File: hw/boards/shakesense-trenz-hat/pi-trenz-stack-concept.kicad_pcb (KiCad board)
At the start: 8 copper layers, 85 x 56 mm, 102 parts, among them J1 Raspberry Pi 40-pin, J2 Passive GNSS antenna, J4 FPGA test UART/reset, J80 LSHM-150-04.0-L-DV-A-S-K-TR, J81 LSHM-150-04.0-L-DV-A-S-K-TR, J82 LSHM-130-04.0-L-DV-A-S-K-TR, J83 1715721, J84 TSW-106-07-G-S, J85 TSW-103-07-G-D, J86 BANK13 / 40p FFC, J87 BANK14 / 40p FFC, J88 BANK15 / 60p FFC, J89 BANK16 / 60p FFC, Q1 2N7002, U1 24LC32A, U11 LSM6DSOTR, U12 LSM6DSOTR, U13 LSM6DSOTR, U14 LSM6DSOTR, U20 SCL3300-D01, U21 MAX-M10S, U40 TLV1117LV33DCYR, U41 SN74LVC8T245PWR, U42 SN74LVC8T245PWR, U43 ISO1640BDR, U51 TXU0202DCUR, U52 TLV803EA30DBZR

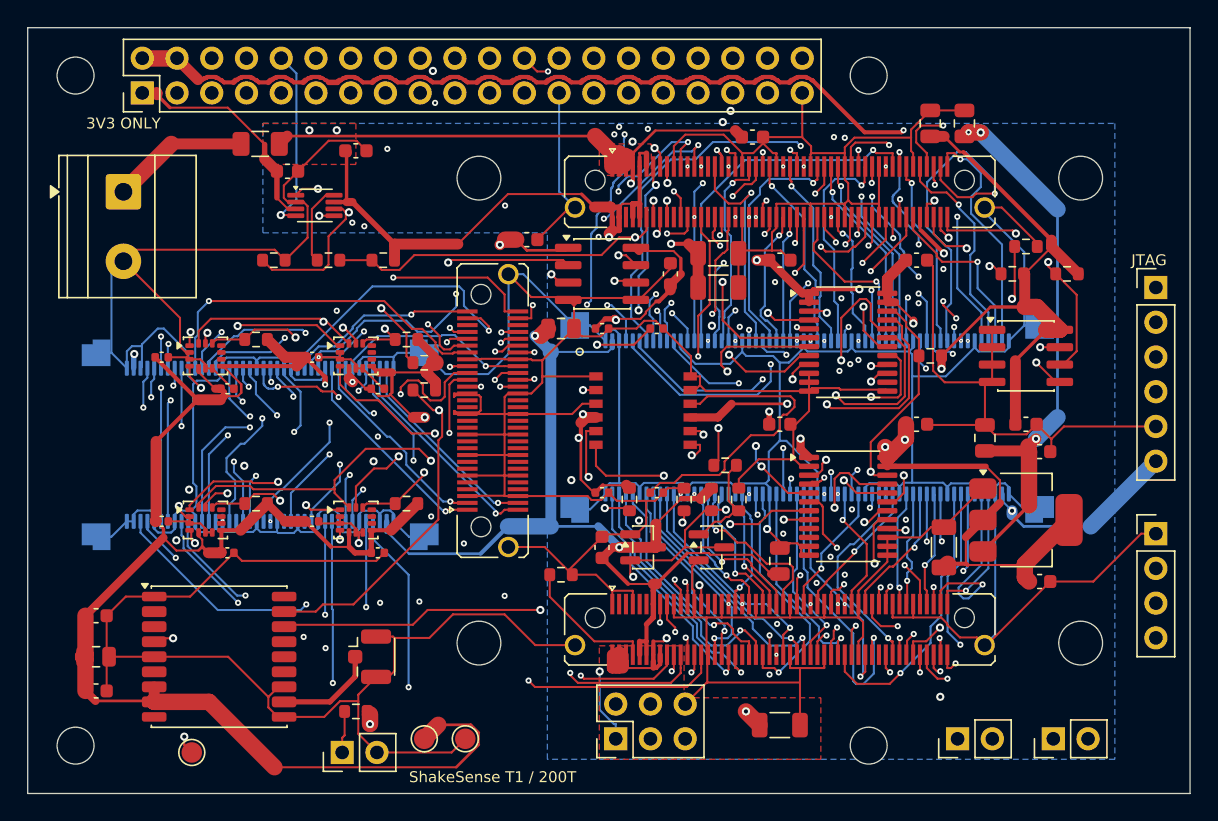
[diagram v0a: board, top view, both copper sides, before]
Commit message: Replace T1 GNSS with single Racotech geophone input
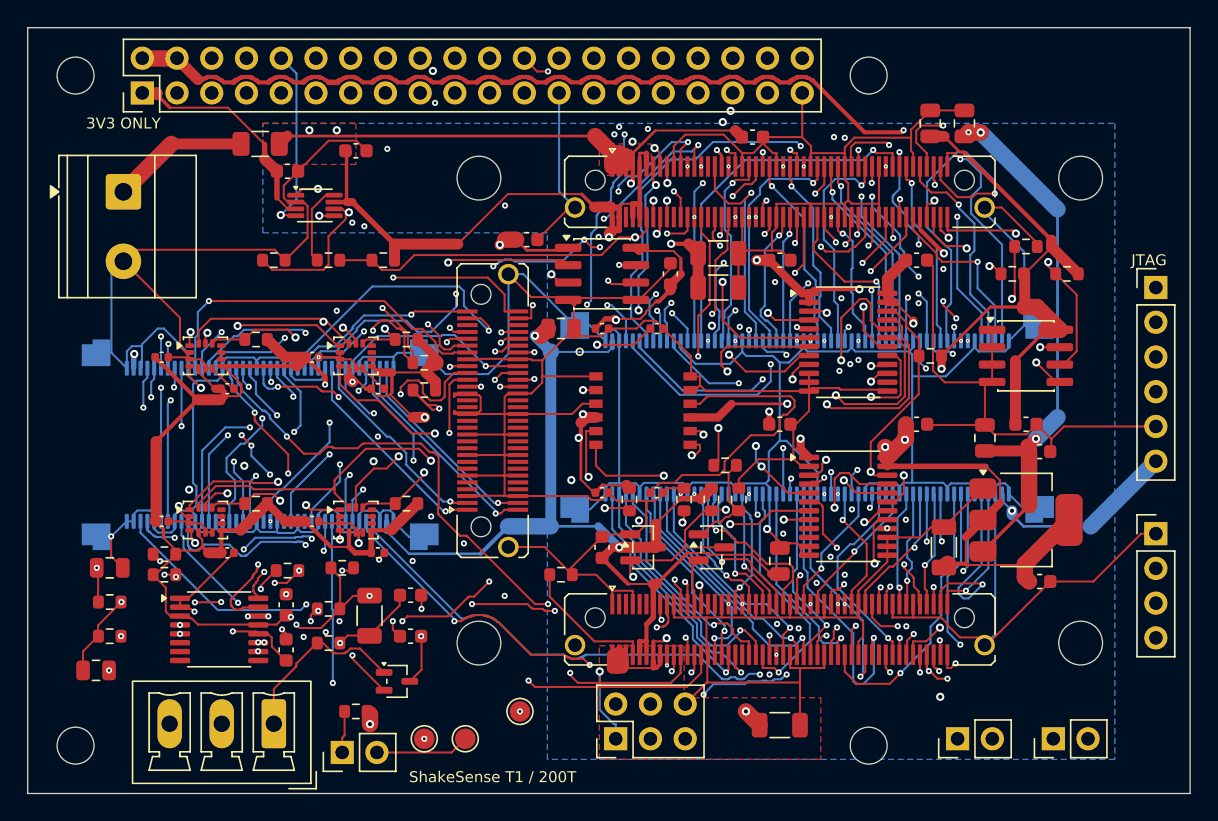
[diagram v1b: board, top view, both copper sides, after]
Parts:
- removed C24, C26: 100n, ShakeSense:Capacitor_SMD__C_0603_1608Metric
- removed C25: 4.7u, ShakeSense:Capacitor_SMD__C_0805_2012Metric
- removed J2: Passive GNSS antenna, ShakeSense:Connector_Coaxial__U.FL_Hirose_U.FL-R-SMT-1_Vertical
- removed U21: MAX-M10S, ShakeSense:RF_GPS__ublox_MAX
- added C90: 100n C0G, ShakeSense:Capacitor_SMD__C_1206_3216Metric, F.Cu at (75.0, 93.0)
- added C91: 1n C0G, ShakeSense:Capacitor_SMD__C_0603_1608Metric, F.Cu at (78.0, 91.5)
- added C92: 1n C0G, ShakeSense:Capacitor_SMD__C_0603_1608Metric, F.Cu at (78.0, 94.5)
- added C93: 10u, ShakeSense:Capacitor_SMD__C_0805_2012Metric, F.Cu at (55.0, 97.0)
- added C94: 10u, ShakeSense:Capacitor_SMD__C_0805_2012Metric, F.Cu at (56.0, 89.5)
- added C95: 100n, ShakeSense:Capacitor_SMD__C_0603_1608Metric, F.Cu at (68.9, 95.5)
- added C96: 100n, ShakeSense:Capacitor_SMD__C_0603_1608Metric, F.Cu at (68.9, 92.2)
- added D90: TPD2E2U06, ShakeSense:Package_TO_SOT_SMD__SOT-323_SC-70, F.Cu at (77.0, 97.8)
- added J90: GEO + / - / SHIELD, ShakeSense:Connector_Phoenix_MC__PhoenixContact_MCV_1,5_3-G-3.81_1x03_P3.81mm_Vertical, F.Cu at (68.0, 100.9)
- added R90: 1k, ShakeSense:Resistor_SMD__R_0603_1608Metric, F.Cu at (72.0, 95.0)
- added R91: 1k, ShakeSense:Resistor_SMD__R_0603_1608Metric, F.Cu at (72.0, 92.5)
- added R92: 1M, ShakeSense:Resistor_SMD__R_0603_1608Metric, F.Cu at (69.0, 89.7)
- added R93: 1M, ShakeSense:Resistor_SMD__R_0603_1608Metric, F.Cu at (73.0, 89.5)
- added R94: 10k, ShakeSense:Resistor_SMD__R_0603_1608Metric, F.Cu at (56.0, 92.0)
- added R95: 10k, ShakeSense:Resistor_SMD__R_0603_1608Metric, F.Cu at (56.0, 94.5)
- added R96: 22, ShakeSense:Resistor_SMD__R_0603_1608Metric, F.Cu at (60.0, 90.0)
- added R97: 10k, ShakeSense:Resistor_SMD__R_0603_1608Metric, F.Cu at (60.0, 88.5)
- added U22: ADS122C04, ShakeSense:Package_SO__TSSOP-16_4.4x5mm_P0.65mm, F.Cu at (64.0, 94.0)
- moved TP4 24.2 mm to (86.0, 100.0)
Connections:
- net PI_GNSS_PPS renamed PI_GEO_DRDY_N
- U42 pad 16: GNSS_PPS -> GEO_DRDY_N
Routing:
- net GEO_DRDY_N: track 0.00 -> 66.6 mm, vias 0 -> 7
- net GNSS_PPS: track 61.5 -> 0.00 mm, vias 2 -> 0
- net GND: track 873.3 -> 819.5 mm, vias 5 -> 16
- net FPGA_B14_L18_P: track 60.1 -> 107.0 mm, vias 2 -> 4
- net SENSOR_OE_N: track 119.2 -> 85.3 mm, vias 3 -> 2
- net GEO_VCM: track 0.00 -> 24.6 mm, vias 0 -> 6
- net SENS_3V3: track 262.7 -> 240.1 mm, vias 10 -> 13
- net GEO_AVDD: track 0.00 -> 19.9 mm, vias 0 -> 4
- net GEO_N: track 0.00 -> 19.5 mm, vias 0 -> 3
- net GEO_AIN_P: track 0.00 -> 18.3 mm, vias 0 -> 4
- net GEO_AIN_N: track 0.00 -> 17.4 mm, vias 0 -> 4
- net I2C_SDA: track 76.0 -> 59.4 mm, vias 3 -> 7
- net GEO_P: track 0.00 -> 13.3 mm
- net FPGA_B14_L24_P: track 73.6 -> 65.6 mm, vias 2 -> 4
- net GNSS_RF: track 7.42 -> 0.00 mm
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
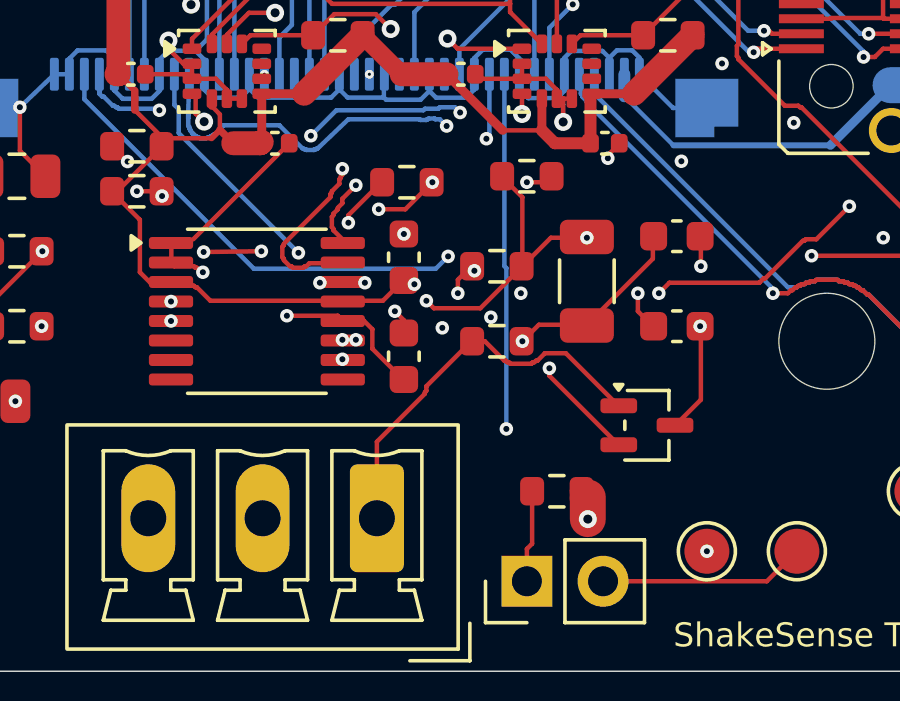
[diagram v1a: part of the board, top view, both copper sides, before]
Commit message: Harden geophone acquisition and tighten analog layout
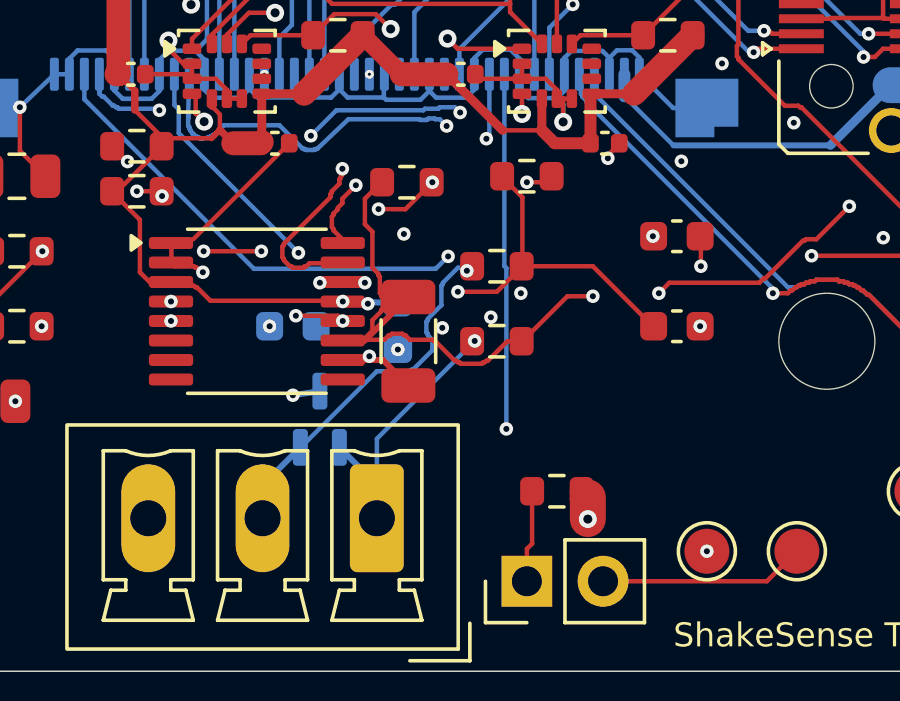
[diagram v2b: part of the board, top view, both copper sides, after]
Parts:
- C95, C96, D90: moved to B.Cu
- moved D90 10.9 mm to (66.1, 97.6), turned to 90 degrees
- moved C90 6.28 mm to (69.0, 95.0), turned to -90 degrees
- moved C95 3.83 mm to (65.2, 94.5), turned to 180 degrees
- moved C96 2.31 mm to (68.7, 94.5), turned to -90 degrees
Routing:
- net GND: track 819.5 -> 813.0 mm, vias 16 -> 18
- net GEO_N: track 19.5 -> 14.3 mm, vias 3 -> 1
- net GEO_P: track 13.3 -> 9.19 mm, vias 0 -> 1
- net GEO_AIN_P: track 18.3 -> 20.8 mm, vias 4 -> 2
- net GEO_AVDD: track 19.9 -> 17.4 mm, vias 4 -> 5
- net SENS_3V3: track 240.1 -> 241.4 mm, vias 13 -> 14
- net GEO_AIN_N: track 17.4 -> 18.0 mm, vias 4 -> 2

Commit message: Resolve T1 ribbon clearance with guided flex and windowed support
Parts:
- added MODEL_OFFSET_SPACER: Visualization only, , F.Cu at (50.0, 50.0)
- moved J87 3.00 mm to (67.0, 86.0)
- moved J83 2.30 mm to (54.7, 62.0)
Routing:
- net GND: track 813.0 -> 868.5 mm, vias 18 -> 30
- net FPGA_B14_L4_N: track 49.4 -> 82.5 mm, vias 3 -> 7
- net FPGA_B13_L6_P: track 44.1 -> 59.4 mm
- net FPGA_B14_L4_P: track 49.6 -> 64.1 mm, vias 2 -> 4
- net FPGA_3V3: track 227.7 -> 241.5 mm, vias 6 -> 8
- net FPGA_B14_L11_P: track 42.6 -> 53.5 mm, vias 3 -> 5
- net FPGA_B14_L5_P: track 22.1 -> 31.4 mm
- net FPGA_B13_L3_P: track 51.8 -> 60.8 mm, vias 6 -> 5
- net FPGA_B14_L14_P: track 57.6 -> 48.9 mm, vias 3 -> 5
- net FPGA_B14_L18_N: track 59.2 -> 66.7 mm, vias 2 -> 5
- net FPGA_B14_L18_P: track 107.0 -> 112.0 mm, vias 4 -> 6
- net FPGA_B14_L9_N: track 58.3 -> 62.2 mm
- net FPGA_B14_L9_P: track 57.4 -> 61.2 mm
- net FPGA_B14_L24_N: track 66.8 -> 70.3 mm
- net FPGA_B14_L15_P: track 53.5 -> 50.1 mm
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
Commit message: Implement internal Pi FPGA link and remove ribbon expansion
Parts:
- removed J84: TSW-106-07-G-S, ShakeSense:TZ_TZ_JTAG
- removed J85: TSW-103-07-G-D, ShakeSense:TZ_TZ_AUX
- removed J86: BANK13 / 40p FFC, ShakeSense:TZ_FFC40
- removed J87: BANK14 / 40p FFC, ShakeSense:TZ_FFC40
- removed J88: BANK15 / 60p FFC, ShakeSense:TZ_FFC60
- removed J89: BANK16 / 60p FFC, ShakeSense:TZ_FFC60
- removed MODEL_OFFSET_SPACER: Visualization only, 
- added C100: 100n, ShakeSense:Capacitor_SMD__C_0603_1608Metric, B.Cu at (106.0, 69.7)
- added C101: 100n, ShakeSense:Capacitor_SMD__C_0603_1608Metric, B.Cu at (106.0, 81.7)
- added C102: 100n, ShakeSense:Capacitor_SMD__C_0603_1608Metric, B.Cu at (73.0, 69.7)
- added C103: 100n, ShakeSense:Capacitor_SMD__C_0603_1608Metric, B.Cu at (84.8, 71.7)
- added C104: 100n, ShakeSense:Capacitor_SMD__C_0603_1608Metric, B.Cu at (77.5, 80.0)
- added C105: 100n, ShakeSense:Capacitor_SMD__C_0603_1608Metric, B.Cu at (84.5, 80.0)
- added C106: , ShakeSense:Capacitor_SMD__C_0603_1608Metric, B.Cu at (79.0, 90.0)
- added R100: 22, ShakeSense:Resistor_SMD__R_0603_1608Metric, B.Cu at (99.0, 58.0)
- added R101: 22, ShakeSense:Resistor_SMD__R_0603_1608Metric, B.Cu at (94.0, 58.0)
- added R102: 22, ShakeSense:Resistor_SMD__R_0603_1608Metric, B.Cu at (89.0, 58.0)
- added R103: 22, ShakeSense:Resistor_SMD__R_0603_1608Metric, B.Cu at (84.0, 58.0)
- added R104: 22, ShakeSense:Resistor_SMD__R_0603_1608Metric, B.Cu at (79.0, 58.0)
- added R105: 22, ShakeSense:Resistor_SMD__R_0603_1608Metric, B.Cu at (74.0, 58.0)
- added R106: 10k, ShakeSense:Resistor_SMD__R_0603_1608Metric, B.Cu at (79.0, 68.0)
- added R107: 10k, ShakeSense:Resistor_SMD__R_0603_1608Metric, B.Cu at (79.0, 70.0)
- added R108: 10k, ShakeSense:Resistor_SMD__R_0603_1608Metric, B.Cu at (88.0, 72.0)
- added R109: 10k, ShakeSense:Resistor_SMD__R_0603_1608Metric, B.Cu at (74.0, 83.0)
- added R110: 10k, ShakeSense:Resistor_SMD__R_0603_1608Metric, B.Cu at (81.0, 83.0)
- added R111: 10k, ShakeSense:Resistor_SMD__R_0603_1608Metric, B.Cu at (94.0, 81.0)
- added R112: 100k, ShakeSense:Resistor_SMD__R_0603_1608Metric, B.Cu at (94.0, 69.0)
- added R113: 10k, ShakeSense:Resistor_SMD__R_0603_1608Metric, B.Cu at (94.0, 75.0)
- added R114: 100k, ShakeSense:Resistor_SMD__R_0603_1608Metric, B.Cu at (94.0, 71.0)
- added R115: 10k, ShakeSense:Resistor_SMD__R_0603_1608Metric, B.Cu at (94.0, 73.0)
- added R116: 100k, ShakeSense:Resistor_SMD__R_0603_1608Metric, B.Cu at (106.0, 75.0)
- added R117: 100k, ShakeSense:Resistor_SMD__R_0603_1608Metric, B.Cu at (94.0, 85.0)
- added U100: TMUX1574PWR, ShakeSense:Package_SO__TSSOP-16_4.4x5mm_P0.65mm, B.Cu at (100.0, 72.0)
- added U101: TMUX1574PWR, ShakeSense:Package_SO__TSSOP-16_4.4x5mm_P0.65mm, B.Cu at (100.0, 84.0)
- added U102: TCA9534PWR, ShakeSense:Package_SO__TSSOP-16_4.4x5mm_P0.65mm, B.Cu at (67.0, 72.0)
- added U103: SN74LVC1G10DCKR, ShakeSense:Package_TO_SOT_SMD__SOT-363_SC-70-6, B.Cu at (81.0, 72.0)
- added U104: TLV809EA30DBZR, ShakeSense:Package_TO_SOT_SMD__SOT-23, B.Cu at (74.0, 80.0)
- added U105: TLV809EA30DBZR, ShakeSense:Package_TO_SOT_SMD__SOT-23, B.Cu at (81.0, 80.0)
- added U106: , ShakeSense:Package_TO_SOT_SMD__SOT-353_SC-70-5, B.Cu at (75.5, 90.0)
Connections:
- J1 pad 12: 12 -> PI_LINK_CS_N
- J1 pad 32: 32 -> PI_LINK_DQ3
- J1 pad 35: 35 -> PI_LINK_DQ1
- J1 pad 36: 36 -> PI_LINK_DQ2
- J1 pad 38: 38 -> PI_LINK_DQ0
- J1 pad 40: 40 -> PI_LINK_SCLK
- J80 pad 100: FPGA_B14_L24_N -> 100
- J80 pad 15: FPGA_B13_L6_N -> 15
- J80 pad 17: FPGA_B13_L6_P -> 17
- J80 pad 18: FPGA_B13_L3_P -> 18
- J80 pad 20: FPGA_B13_L3_N -> 20
- J80 pad 21: FPGA_B13_L5_N -> 21
- J80 pad 22: FPGA_B13_L11_N -> 22
- J80 pad 23: FPGA_B13_L5_P -> 23
- J80 pad 24: FPGA_B13_L11_P -> 24
- J80 pad 26: FPGA_B13_L9_N -> 26
- J80 pad 28: FPGA_B13_L9_P -> 28
- J80 pad 32: FPGA_B16_L22_P -> 32
- J80 pad 34: FPGA_B16_L22_N -> 34
- J80 pad 35: FPGA_B16_L16_P -> 35
- J80 pad 36: FPGA_B16_L24_N -> 36
- J80 pad 37: FPGA_B16_L16_N -> 37
- J80 pad 38: FPGA_B16_L24_P -> 38
- J80 pad 39: FPGA_B16_L19_N -> 39
- J80 pad 40: j80-40 -> 40
- J80 pad 41: FPGA_B16_L19_P -> 41
- J80 pad 42: FPGA_B16_L23_P -> 42
- J80 pad 44: FPGA_B16_L23_N -> 44
- J80 pad 45: FPGA_B16_L17_N -> 45
- J80 pad 46: FPGA_B16_L15_P -> 46
- J80 pad 47: FPGA_B16_L17_P -> 47
- J80 pad 48: FPGA_B16_L15_N -> 48
- J80 pad 49: FPGA_B16_L18_N -> 49
- J80 pad 50: FPGA_B16_L20_P -> 50
- J80 pad 51: FPGA_B16_L18_P -> 51
- J80 pad 52: FPGA_B16_L20_N -> 52
- J80 pad 55: FPGA_B16_L9_N -> 55
- J80 pad 56: FPGA_B16_L21_P -> 56
- J80 pad 57: FPGA_B16_L9_P -> 57
- J80 pad 58: FPGA_B16_L21_N -> 58
- J80 pad 59: FPGA_B16_L7_N -> 59
- J80 pad 60: FPGA_B16_L13_P -> 60
- J80 pad 61: FPGA_B16_L7_P -> 61
- J80 pad 62: FPGA_B16_L13_N -> 62
- J80 pad 65: FPGA_B16_L11_P -> 65
- J80 pad 66: FPGA_B16_L14_P -> 66
- J80 pad 67: FPGA_B16_L11_N -> 67
- J80 pad 68: FPGA_B16_L14_N -> 68
- J80 pad 69: FPGA_B16_L10_N -> 69
- J80 pad 70: FPGA_B16_L3_N -> 70
- J80 pad 71: FPGA_B16_L10_P -> 71
- J80 pad 72: FPGA_B16_L3_P -> 72
- J80 pad 75: FPGA_B16_L5_N -> 75
- J80 pad 76: FPGA_B16_L12_P -> 76
- J80 pad 77: FPGA_B16_L5_P -> 77
- J80 pad 78: FPGA_B16_L12_N -> 78
- J80 pad 79: FPGA_B16_L2_N -> 79
- J80 pad 81: FPGA_B16_L2_P -> 81
- J80 pad 82: FPGA_B16_L8_N -> 82
- J80 pad 84: FPGA_B16_L8_P -> 84
- J80 pad 85: FPGA_B16_L6_N -> 85
- J80 pad 86: FPGA_B14_L18_N -> 86
- J80 pad 87: FPGA_B16_L6_P -> 87
- J80 pad 88: FPGA_B14_L18_P -> 88
- J80 pad 91: FPGA_B14_L24_P -> 91
- J80 pad 92: FPGA_B14_L9_P -> 92
- J80 pad 93: FPGA_B16_L4_N -> 93
- J80 pad 94: FPGA_B14_L9_N -> 94
- J80 pad 95: FPGA_B16_L4_P -> 95
- J80 pad 96: FPGA_B14_L4_P -> 96
- J80 pad 97: FPGA_B16_L1_N -> 97
- J80 pad 98: FPGA_B14_L4_N -> 98
- J80 pad 99: FPGA_B16_L1_P -> 99
- J81 pad 15: FPGA_AUX0 -> j81-15
- J81 pad 16: FPGA_AUX1 -> 16
- J81 pad 18: FPGA_AUX2 -> j81-18
- J81 pad 20: 20 -> j81-20
- J81 pad 21: FPGA_B14_L12_P -> FPGA_LINK_SCLK
- J81 pad 22: FPGA_B14_L14_P -> FPGA_LINK_DQ0
- J81 pad 23: FPGA_B14_L12_N -> FPGA_LINK_CS_N
- J81 pad 24: FPGA_B14_L14_N -> FPGA_LINK_DQ1
- J81 pad 25: FPGA_B14_L11_P -> 25
- J81 pad 26: FPGA_B14_L13_P -> FPGA_LINK_DQ2
- J81 pad 27: FPGA_B14_L11_N -> 27
- J81 pad 28: FPGA_B14_L13_N -> FPGA_LINK_DQ3
- J81 pad 31: FPGA_B15_L9_N -> 31
- J81 pad 32: FPGA_B14_L16_P -> j81-32
- J81 pad 33: FPGA_B15_L9_P -> 33
- J81 pad 34: FPGA_B14_L16_N -> j81-34
- J81 pad 35: FPGA_B15_L8_N -> j81-35
- J81 pad 36: FPGA_B14_L15_P -> j81-36
- J81 pad 37: FPGA_B15_L8_P -> j81-37
- J81 pad 38: FPGA_B14_L15_N -> j81-38
- J81 pad 41: FPGA_B15_L7_N -> j81-41
- J81 pad 42: FPGA_B15_L23_P -> j81-42
- J81 pad 43: FPGA_B15_L7_P -> 43
- J81 pad 44: FPGA_B15_L23_N -> j81-44
- J81 pad 45: FPGA_B15_L13_P -> j81-45
- J81 pad 46: FPGA_B15_L19_P -> j81-46
- J81 pad 47: FPGA_B15_L13_N -> j81-47
- J81 pad 48: FPGA_B15_L19_N -> j81-48
- J81 pad 51: FPGA_B15_L14_P -> j81-51
- J81 pad 52: FPGA_B15_L11_P -> j81-52
- J81 pad 53: FPGA_B15_L14_N -> 53
- J81 pad 54: FPGA_B15_L11_N -> 54
- J81 pad 55: FPGA_B15_L12_P -> j81-55
- J81 pad 56: FPGA_B15_L3_P -> j81-56
- J81 pad 57: FPGA_B15_L12_N -> j81-57
- J81 pad 58: FPGA_B15_L3_N -> j81-58
- J81 pad 61: FPGA_B15_L10_N -> j81-61
- J81 pad 62: FPGA_B15_L17_N -> j81-62
- J81 pad 63: FPGA_B15_L10_P -> 63
- J81 pad 64: FPGA_B15_L17_P -> 64
- J81 pad 65: FPGA_B15_L18_P -> j81-65
- J81 pad 66: FPGA_B15_L16_P -> j81-66
- J81 pad 67: FPGA_B15_L18_N -> j81-67
- J81 pad 68: FPGA_B15_L16_N -> j81-68
- J81 pad 71: FPGA_B15_L20_P -> j81-71
- J81 pad 72: FPGA_B15_L1_P -> j81-72
- J81 pad 73: FPGA_B15_L20_N -> 73
- J81 pad 74: FPGA_B15_L1_N -> 74
- J81 pad 75: FPGA_B15_L15_P -> j81-75
- J81 pad 76: FPGA_B15_L2_N -> j81-76
- J81 pad 77: FPGA_B15_L15_N -> j81-77
- J81 pad 78: FPGA_B15_L2_P -> j81-78
- J81 pad 81: FPGA_B15_L6_N -> j81-81
- J81 pad 82: FPGA_B15_L4_P -> j81-82
- J81 pad 83: FPGA_B15_L6_P -> 83
- J81 pad 84: FPGA_B15_L4_N -> j81-84
- J81 pad 85: FPGA_B15_L21_P -> j81-85
- J81 pad 86: FPGA_B15_L5_N -> j81-86
- J81 pad 87: FPGA_B15_L21_N -> j81-87
- J81 pad 88: FPGA_B15_L5_P -> j81-88
- J81 pad 90: FPGA_B15_IO0 -> 90
- J81 pad 91: FPGA_B15_L24_N -> j81-91
- J81 pad 93: FPGA_B15_L24_P -> j81-93
- J81 pad 95: FPGA_B15_L22_N -> j81-95
- J81 pad 97: FPGA_B15_L22_P -> j81-97
- J81 pad 99: FPGA_B15_IO25 -> j81-99
- J82 pad 1: FPGA_B13_L14_P -> 1
- J82 pad 15: 15 -> j82-15
- J82 pad 16: 16 -> j82-16
- J82 pad 2: FPGA_B13_L17_P -> 2
- J82 pad 21: 21 -> j82-21
- J82 pad 22: 22 -> j82-22
- J82 pad 25: 25 -> j82-25
- J82 pad 26: 26 -> j82-26
- J82 pad 27: 27 -> j82-27
- J82 pad 28: 28 -> j82-28
- J82 pad 3: FPGA_B13_L14_N -> j82-3
- J82 pad 31: 31 -> j82-31
- J82 pad 33: 33 -> j82-33
- J82 pad 34: 34 -> j82-34
- J82 pad 37: FPGA_B13_L16_P -> j82-37
- J82 pad 38: FPGA_B13_L10_P -> j82-38
- J82 pad 39: FPGA_B13_L16_N -> j82-39
- J82 pad 4: FPGA_B13_L17_N -> 4
- J82 pad 40: FPGA_B13_L10_N -> j82-40
- J82 pad 41: FPGA_B13_L1_P -> j82-41
- J82 pad 42: FPGA_B13_L15_P -> j82-42
- J82 pad 43: FPGA_B13_L1_N -> j82-43
- J82 pad 44: FPGA_B13_L15_N -> j82-44
- J82 pad 47: FPGA_B13_L4_P -> j82-47
- J82 pad 48: FPGA_B14_L5_P -> j82-48
- J82 pad 49: FPGA_B13_L4_N -> j82-49
- J82 pad 50: FPGA_B14_L5_N -> j82-50
- J82 pad 51: FPGA_B13_L2_N -> j82-51
- J82 pad 52: FPGA_B14_L20_P -> j82-52
- J82 pad 53: FPGA_B13_L2_P -> j82-53
- J82 pad 54: FPGA_B14_L20_N -> j82-54
- J82 pad 55: 55 -> j82-55
- J82 pad 56: 56 -> j82-56
- J82 pad 57: FPGA_B13_L12_P -> j82-57
- J82 pad 58: FPGA_B13_L13_P -> j82-58
- J82 pad 59: FPGA_B13_L12_N -> j82-59
- J82 pad 60: FPGA_B13_L13_N -> j82-60
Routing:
- net FPGA_B14_L18_P: track 112.0 -> 0.00 mm, vias 6 -> 0
- net GND: track 868.5 -> 781.2 mm, vias 30 -> 55
- net FPGA_B14_L4_N: track 82.5 -> 0.00 mm, vias 7 -> 0
- net FPGA_B14_L24_N: track 70.3 -> 0.00 mm, vias 2 -> 0
- net FPGA_B14_L24_P: track 68.4 -> 0.00 mm, vias 6 -> 0
- net FPGA_B14_L18_N: track 66.7 -> 0.00 mm, vias 5 -> 0
- net FPGA_B14_L4_P: track 64.1 -> 0.00 mm, vias 4 -> 0
- net LINK_JTAG_SEL: track 0.00 -> 62.8 mm, vias 0 -> 4
- net FPGA_B14_L9_N: track 62.2 -> 0.00 mm, vias 5 -> 0
- net FPGA_B14_L9_P: track 61.2 -> 0.00 mm, vias 2 -> 0
- net FPGA_B13_L3_P: track 60.8 -> 0.00 mm, vias 5 -> 0
- net FPGA_B13_L6_P: track 59.4 -> 0.00 mm, vias 5 -> 0
- net FPGA_B13_L5_N: track 57.1 -> 0.00 mm, vias 3 -> 0
- net FPGA_B14_L15_N: track 56.7 -> 0.00 mm, vias 5 -> 0
- net FPGA_AUX2: track 55.5 -> 0.00 mm, vias 1 -> 0
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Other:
- board text removed: "GPIO J86 B13 3V3"
- board text removed: "GPIO J87 B14 3V3"
- board text removed: "GPIO J88 B15 3V3"
- board text removed: "GPIO J89 B16 3V3"
- board text removed: "JTAG"
